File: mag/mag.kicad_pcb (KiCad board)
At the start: 2 copper layers, 24 parts, among them K1 кнопка_FSMSM, K2 кнопка_FSMSM

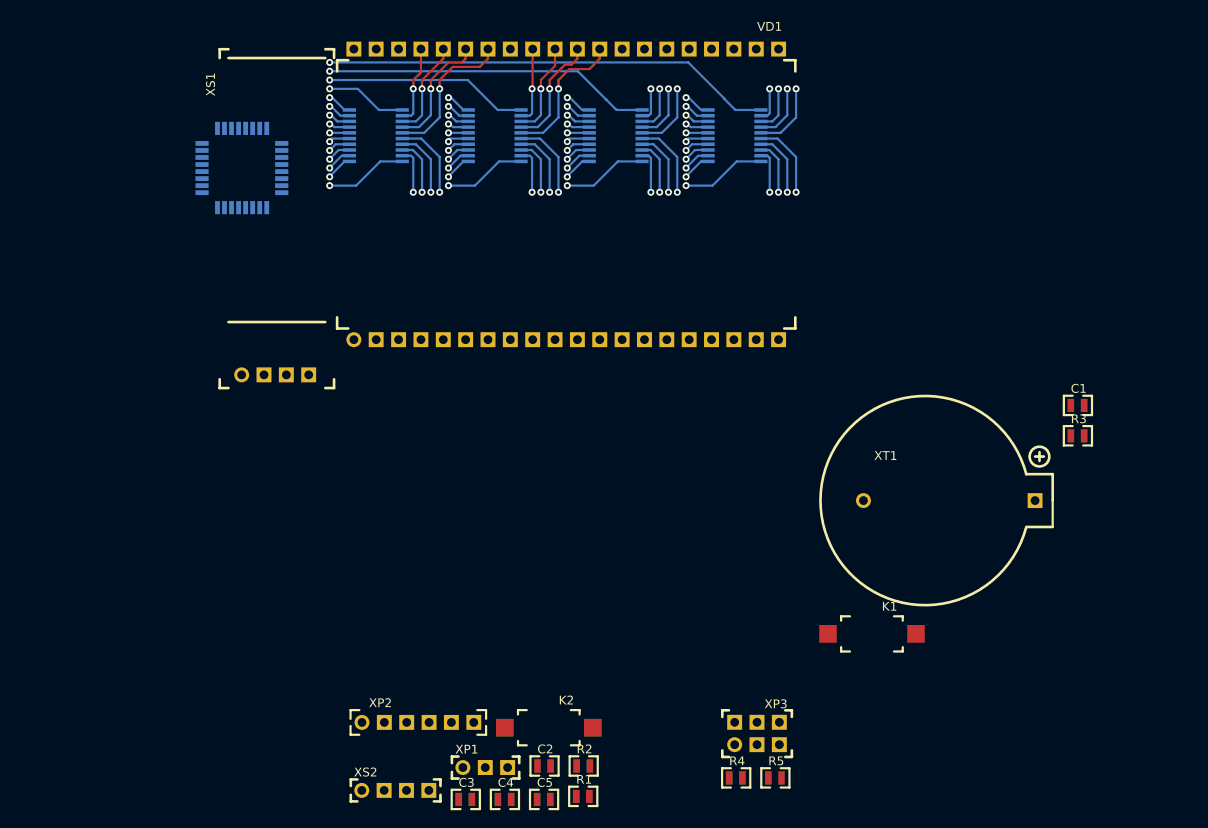
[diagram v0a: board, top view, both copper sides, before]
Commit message: есть топология и габарит, не расставлен обвес
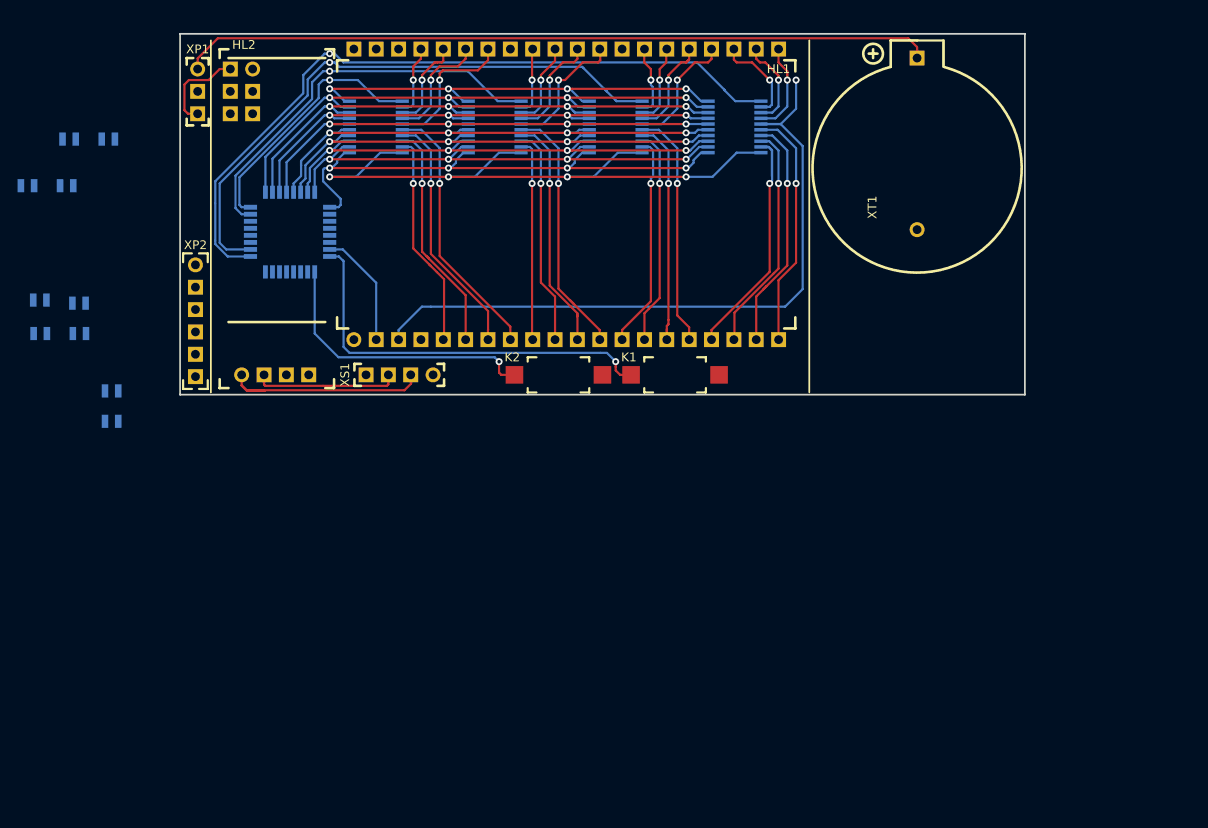
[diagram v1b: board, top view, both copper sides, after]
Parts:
- removed VD1: display_EDS803_EDS805, N_VD_HL:display_EDS803_805
- removed the XS1 at (105.0, 79.0)
- added HL1: display_EDS803_EDS805, N_VD_HL:display_EDS803_805, F.Cu at (117.8, 75.0)
- added HL2: oled_0.91_128x32, N_VD_HL:oled_0.91_128x32, F.Cu at (105.0, 79.0)
- C1, C2, C3, C4, C5, R1, R2, R3, R4, R5, XP3: moved to B.Cu
- moved R3 109.9 mm to (89.5, 80.8)
- moved C1 109.8 mm to (89.5, 84.3)
- moved R4 104.9 mm to (84.6, 52.2)
- moved R5 104.9 mm to (89.1, 52.2)
- moved XP3 94.3 mm to (106.2, 44.2), turned to 270 degrees
- moved C4 85.7 mm to (84.4, 57.5)
- moved C3 85.7 mm to (79.9, 57.5)
- moved XP1 84.9 mm to (100.0, 44.2), turned to 270 degrees
- moved C5 80.6 mm to (81.3, 70.5)
- moved R1 80.1 mm to (85.8, 70.9)
- moved C2 75.4 mm to (81.4, 74.3)
- moved R2 75.4 mm to (85.8, 74.3)
- moved XP2 55.3 mm to (99.8, 66.5), turned to 270 degrees
- moved XS1 47.9 mm to (126.8, 79.0), turned to 180 degrees
- moved K2 40.1 mm to (136.0, 79.0)
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- renumbered XS2 to XS1
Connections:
- DD2 pad 1: /PB3_MOSI -> /PB5_SCK
- DD2 pad 11: /PC0 -> /PB7
- DD2 pad 2: /PB6 -> /PB4_MISO
- DD2 pad 3: /PB7 -> /PB3_MOSI
- DD2 pad 4: /PD5 -> /PB2
- DD2 pad 5: /PD6 -> /PB1
- DD2 pad 6: /PD7 -> /PB0
- DD2 pad 7: /PB0 -> /PD7
- DD2 pad 8: /PB1 -> /PD6
- DD2 pad 9: /PB2 -> /PD5
- DD3 pad 1: /PB3_MOSI -> /PB5_SCK
- DD3 pad 11: /PC1 -> /PB6
- DD3 pad 2: /PB6 -> /PB4_MISO
- DD3 pad 3: /PB7 -> /PB3_MOSI
- DD3 pad 4: /PD5 -> /PB2
- DD3 pad 5: /PD6 -> /PB1
- DD3 pad 6: /PD7 -> /PB0
- DD3 pad 7: /PB0 -> /PD7
- DD3 pad 8: /PB1 -> /PD6
- DD3 pad 9: /PB2 -> /PD5
- DD4 pad 1: /PB3_MOSI -> /PB5_SCK
- DD4 pad 11: /PC2 -> /PD4
- DD4 pad 2: /PB6 -> /PB4_MISO
- DD4 pad 3: /PB7 -> /PB3_MOSI
- DD4 pad 4: /PD5 -> /PB2
- DD4 pad 5: /PD6 -> /PB1
- DD4 pad 6: /PD7 -> /PB0
- DD4 pad 7: /PB0 -> /PD7
- DD4 pad 8: /PB1 -> /PD6
- DD4 pad 9: /PB2 -> /PD5
- DD5 pad 1: /PB3_MOSI -> /PB5_SCK
- DD5 pad 11: /PC3 -> /PD3
- DD5 pad 2: /PB6 -> /PB4_MISO
- DD5 pad 3: /PB7 -> /PB3_MOSI
- DD5 pad 4: /PD5 -> /PB2
- DD5 pad 5: /PD6 -> /PB1
- DD5 pad 6: /PD7 -> /PB0
- DD5 pad 7: /PB0 -> /PD7
- DD5 pad 8: /PB1 -> /PD6
- DD5 pad 9: /PB2 -> /PD5
- K1 pad 1: /PD3 -> /PC1
- K2 pad 1: /PD4 -> /PC2
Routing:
- net /VCC_bat: track 0.00 -> 85.6 mm
- net /PD3: track 0.00 -> 83.0 mm, vias 0 -> 1
- net /Out45: track 8.22 -> 79.2 mm
- net /PD4: track 0.00 -> 67.1 mm, vias 0 -> 1
- net /PB5_SCK: track 0.00 -> 61.4 mm, vias 0 -> 4
- net /PB4_MISO: track 0.00 -> 59.4 mm, vias 0 -> 4
- net /PD5: track 9.99 -> 65.5 mm
- net /PD6: track 9.41 -> 63.6 mm
- net /PD7: track 9.17 -> 61.7 mm
- net /PC3: track 51.0 -> 0.00 mm, vias 1 -> 0
- net /PB0: track 9.75 -> 59.8 mm
- net /PB1: track 10.3 -> 60.1 mm
- net /PB2: track 10.9 -> 60.6 mm
- net /PB3_MOSI: track 12.0 -> 59.9 mm
- net /VCC: track 37.6 -> 78.1 mm
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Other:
- board outline added: 96 x 41 mm
- rule pad_to_mask_clearance: 0.051 -> 0.02
- rule solder_mask_min_width: 0.25 -> 0.02

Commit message: трассировка завершена, требуется маркировка
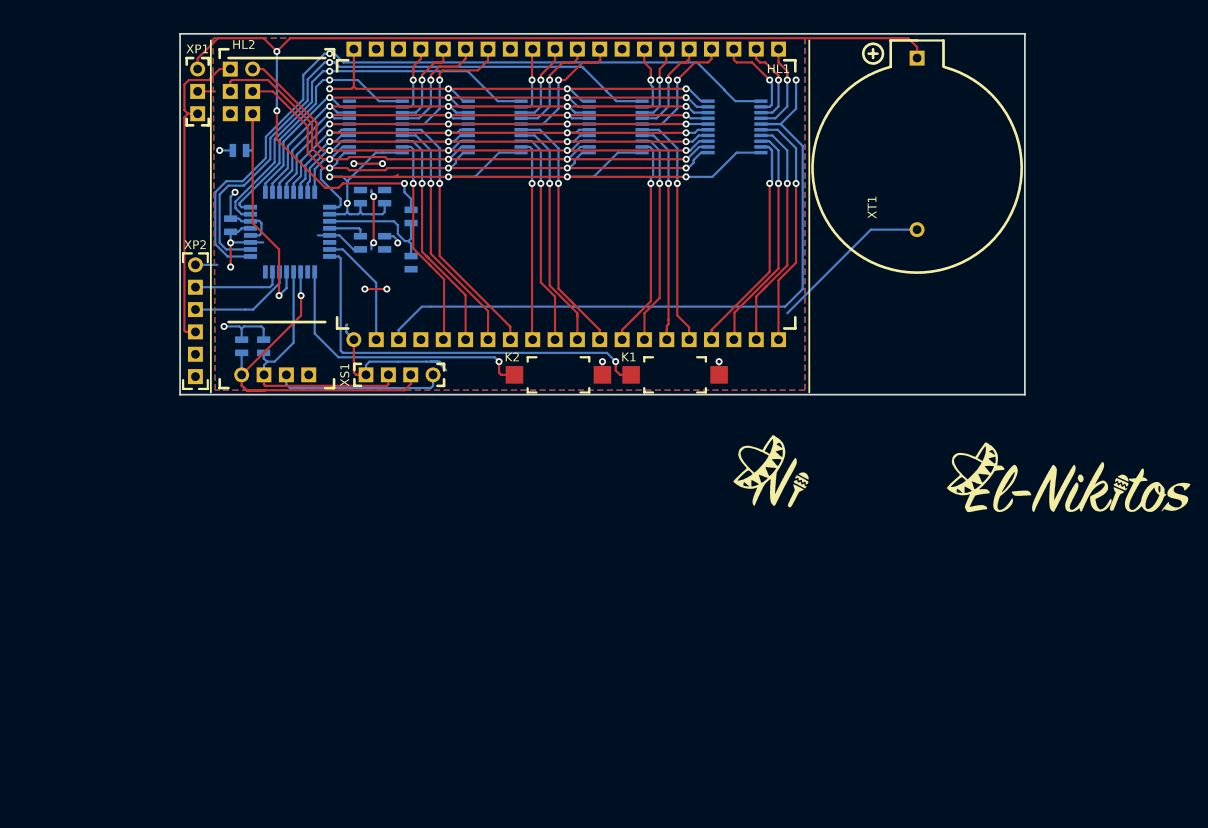
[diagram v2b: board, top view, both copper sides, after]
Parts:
- added G***: LOGO, N_ICO:ni_10x10, F.Cu at (165.8, 90.5)
- added G***: LOGO, N_ICO:el-nikitos_29x10, F.Cu at (199.5, 91.2)
- moved C3 41.4 mm to (121.2, 59.5), turned to 90 degrees
- moved R4 40.4 mm to (124.2, 60.2), turned to 270 degrees
- moved C2 40.0 mm to (118.5, 59.5), turned to 90 degrees
- moved C5 37.9 mm to (118.5, 63.2), turned to 270 degrees
- moved R5 37.6 mm to (124.2, 65.5), turned to 270 degrees
- moved C4 37.3 mm to (121.2, 63.2), turned to 270 degrees
- moved R3 30.9 mm to (104.0, 53.5)
- moved C1 27.1 mm to (103.8, 61.2), turned to 270 degrees
- moved R2 21.7 mm to (107.5, 75.0), turned to 270 degrees
- moved R1 19.7 mm to (105.0, 75.0), turned to 270 degrees
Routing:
- net /GND: track 52.0 -> 126.7 mm, vias 4 -> 14
- net /VCC: track 78.1 -> 132.8 mm, vias 4 -> 9
- net /VCC_bat: track 85.6 -> 117.1 mm, vias 0 -> 3
- net /RES: track 0.00 -> 30.1 mm, vias 0 -> 1
- net /VCC_prog: track 10.6 -> 36.7 mm
- net /PB4_MISO: track 59.4 -> 77.4 mm
- net /SDA: track 24.9 -> 41.9 mm, vias 0 -> 1
- net /PB5_SCK: track 61.4 -> 76.8 mm
- net /SCL: track 16.2 -> 31.0 mm
- net /ADC6: track 0.00 -> 14.5 mm
- net /PB3_MOSI: track 59.9 -> 73.9 mm
- net /MC_RX: track 0.00 -> 12.1 mm
- net /MC_TX: track 0.00 -> 10.3 mm
- net /AREF: track 0.00 -> 4.31 mm
- net /PD3: track 83.0 -> 84.0 mm
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- added copper zone on B.Cu, net /GND
- added copper zone on F.Cu, net /VCC

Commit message: закончена трассировка и маркировка
не подготавливались файлы производства
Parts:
- added G***: LOGO, N_ICO:skyer_25x5, B.Cu at (177.8, 61.0)
- added G***: LOGO, N_ICO:skyer_19x4, B.Cu at (147.0, 78.5)
- G*** (x2): moved to B.Cu
- moved G*** 67.3 mm to (110.5, 52.0), turned to 180 degrees
- moved G*** 33.2 mm to (188.2, 60.0), turned to 270 degrees
- moved R3 1.00 mm to (104.0, 54.5)
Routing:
- net /RES: track 30.1 -> 31.3 mm
- net /GND: track 126.7 -> 127.7 mm
- net /VCC: track 132.8 -> 132.3 mm
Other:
- board text added: "BAT"
- board text added: "CR2032"
- board text added: "GND"
- board text added: "PR"
- board text added: "R"
- board text added: "RX"
- board text added: "SCL"
- board text added: "SDA"
- board text added: "TX"
- board text added: "VCC"
- board text added: "mag.0"
